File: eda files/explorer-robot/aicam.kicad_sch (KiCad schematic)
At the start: 7 parts, among them J8 AI CAM, U9 TPS22917DBV

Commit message: Add expansion connector sheet and hierarchical wiring
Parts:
- J8: value AI CAM -> AI.CAM
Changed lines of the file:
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@@
 			)
 		)
-		(property "Value" "AI CAM"
+		(property "Value" "AI.CAM"
 			(at 187.96 96.5199 0)
 			(show_name no)

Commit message: ``` Move AI camera branch to 3.3 V rail
The Grove Vision AI V2 module used here requires a 3.3 V input,
so powering it from the switched 5 V branch would over-voltage it.
Point U9 VIN at +3.3V; the TPS22917, footprint and control are
unchanged.

Also bump the 5 V inductor to 15 µH/3 A, swap the catch diode,
clean up schematic wiring and add no-connects on unused pins.
Document the decision in ADR-0025 and update ADR-0019, ADR-0021
and CONTEXT.md.
```
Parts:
- added C60: 10u, Capacitor_SMD:C_0805_2012Metric, symbol Device:C
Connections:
- net GND: now also C60.2
- net at C54.2, J8.1 (Pin_1), R20.1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: now also C60.1
- net +5V renamed +3.3V
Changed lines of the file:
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@@
+	)
+	(junction
+		(at 177.8 91.44)
+		(diameter 0)
+		(color 0 0 0 0)
 	)
 	(junction
@@
 	(wire
 		(pts
+			(xy 177.8 90.17) (xy 177.8 91.44)
+		)
+		(stroke
+			(width 0)
+			(type default)
+		)
+	)
+	(wire
+		(pts
 			(xy 123.19 91.44) (xy 135.89 91.44)
 		)
@@
 	(wire
 		(pts
+			(xy 177.8 80.01) (xy 177.8 82.55)
+		)
+		(stroke
+			(width 0)
+			(type default)
+		)
+	)
+	(wire
+		(pts
+			(xy 177.8 91.44) (xy 180.34 91.44)
+		)
+		(stroke
+			(width 0)
+			(type default)
+		)
+	)
+	(wire
+		(pts
 			(xy 167.64 96.52) (xy 167.64 101.6)
 		)
@@
 	(wire
 		(pts
-			(xy 170.18 91.44) (xy 180.34 91.44)
+			(xy 170.18 91.44) (xy 177.8 91.44)
 		)
 		(stroke
@@
 	)
 	(symbol
+		(lib_id "Device:C")
+		(at 177.8 86.36 180)
+		(unit 1)
+		(body_style 1)
+		(exclude_from_sim no)
+		(in_bom yes)
+		(on_board yes)
+		(in_pos_files yes)
+		(dnp no)
+		(property "Reference" "C60"
+			(at 184.912 87.376 0)
+			(show_name no)
+			(do_not_autoplace no)
+			(effects
+				(font
+					(size 1.27 1.27)
+				)
+				(justify left)
+			)
+		)
+		(property "Value" "10u"
+			(at 184.912 84.836 0)
+			(show_name no)
+			(do_not_autoplace no)
+			(effects
+				(font
+					(size 1.27 1.27)
+				)
+				(justify left)
+			)
+		)
+		(property "Footprint" "Capacitor_SMD:C_0805_2012Metric"
+			(at 176.8348 82.55 0)
+			(hide yes)
+			(show_name no)
+			(do_not_autoplace no)
+			(effects
+				(font
+					(size 1.27 1.27)
+				)
+			)
+		)
+		(property "Datasheet" ""
+			(at 177.8 86.36 0)
+			(hide yes)
+			(show_name no)
+			(do_not_autoplace no)
+			(effects
+				(font
+					(size 1.27 1.27)
+				)
+			)
+		)
+		(property "Description" "Unpolarized capacitor"
+			(at 177.8 86.36 0)
+			(hide yes)
+			(show_name no)
+			(do_not_autoplace no)
+			(effects
+				(font
+					(size 1.27 1.27)
+				)
+			)
+		)
+		(property "JLCPCB_URL" "https://jlcpcb.com/partdetail/16532-CL21A106KAYNNNE/C15850"
+			(at 177.8 86.36 0)
+			(hide yes)
+			(show_name no)
+			(do_not_autoplace no)
+			(effects
+				(font
+					(size 1.27 1.27)
+				)
+			)
+		)
+		(property "LCSC" "C15850"
+			(at 177.8 86.36 0)
+			(hide yes)
+			(show_name no)
+			(do_not_autoplace no)
+			(effects
+				(font
+					(size 1.27 1.27)
+				)
+			)
+		)
+		(property "MFR" "Samsung Electro-Mechanics"
+			(at 177.8 86.36 0)
+			(hide yes)
+			(show_name no)
+			(do_not_autoplace no)
+			(effects
+				(font
+					(size 1.27 1.27)
+				)
+			)
+		)
+		(property "MPN" "CL21A106KAYNNNE"
+			(at 177.8 86.36 0)
+			(hide yes)
+			(show_name no)
+			(do_not_autoplace no)
+			(effects
+				(font
+					(size 1.27 1.27)
+				)
+			)
+		)
+		(pin "2"
+		)
+		(pin "1"
+		)
+		(instances
+			(project "explorer-robot"
+				(path "/57778957-dc0c-4e39-b470-8f64ada5e845/e28148a8-209c-4954-97f4-1069761fd156"
+					(reference "C60")
+					(unit 1)
+				)
+			)
+		)
+	)
+	(symbol
+		(lib_id "power:GND")
+		(at 177.8 80.01 180)
+		(unit 1)
+		(body_style 1)
+		(exclude_from_sim no)
+		(in_bom yes)
+		(on_board yes)
+		(in_pos_files yes)
+		(dnp no)
+		(fields_autoplaced yes)
+		(property "Reference" "#PWR094"
+			(at 177.8 73.66 0)
+			(hide yes)
+			(show_name no)
+			(do_not_autoplace no)
+			(effects
+				(font
+					(size 1.27 1.27)
+				)
+			)
+		)
+		(property "Value" "GND"
+			(at 177.8 74.93 0)
+			(show_name no)
+			(do_not_autoplace no)
+			(effects
+				(font
+					(size 1.27 1.27)
+				)
+			)
+		)
+		(property "Footprint" ""
+			(at 177.8 80.01 0)
+			(hide yes)
+			(show_name no)
+			(do_not_autoplace no)
+			(effects
+				(font
+					(size 1.27 1.27)
+				)
+			)
+		)
+		(property "Datasheet" ""
+			(at 177.8 80.01 0)
+			(hide yes)
+			(show_name no)
+			(do_not_autoplace no)
+			(effects
+				(font
+					(size 1.27 1.27)
+				)
+			)
+		)
+		(property "Description" "Power symbol creates a global label with name \"GND\" , ground"
+			(at 177.8 80.01 0)
+			(hide yes)
+			(show_name no)
+			(do_not_autoplace no)
+			(effects
+				(font
+					(size 1.27 1.27)
+				)
+			)
+		)
+		(pin "1"
+		)
+		(instances
+			(project "explorer-robot"
+				(path "/57778957-dc0c-4e39-b470-8f64ada5e845/e28148a8-209c-4954-97f4-1069761fd156"
+					(reference "#PWR094")
+					(unit 1)
+				)
+			)
+		)
+	)
+	(symbol
 		(lib_id "Device:R")
 		(at 160.02 91.44 270)
@@
 	)
 	(symbol
-		(lib_id "power:+5V")
+		(lib_id "power:+3.3V")
 		(at 124.46 86.36 90)
 		(unit 1)
@@
 		(in_pos_files yes)
 		(dnp no)
-		(fields_autoplaced yes)
 		(property "Reference" "#PWR078"
 			(at 128.27 86.36 0)
@@
 			)
 		)
-		(property "Value" "+5V"
-			(at 119.38 86.36 0)
+		(property "Value" "+3.3V"
+			(at 117.602 86.614 90)
 			(show_name no)
 			(do_not_autoplace no)
@@
 			)
 		)
-		(property "Description" "Power symbol creates a global label with name \"+5V\""
+		(property "Description" "Power symbol creates a global label with name \"+3.3V\""
 			(at 124.46 86.36 0)
 			(hide yes)

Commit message: Update AI camera branch to 5V and document schematic
- ADR-0027 supersedes ADR-0025: AI camera input is 5V, not 3.3V
- Move U9 VIN and C55 back to +5V in aicam.kicad_sch
- Update CONTEXT.md branch descriptions and ADR cross-references
- Record ICM-20948 placement status and corrected battery divider ratio
- Adjust battery_charge_read for 33k/10k divider (0.2326 ratio)
- Enable sheet component classes; refresh netlist and PCB footprints
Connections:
- net +3.3V renamed +5V
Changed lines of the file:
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@@
+	)
+	(symbol
+		(lib_id "power:+5V")
+		(at 124.46 86.36 90)
+		(unit 1)
+		(body_style 1)
+		(exclude_from_sim no)
+		(in_bom yes)
+		(on_board yes)
+		(in_pos_files yes)
+		(dnp no)
+		(fields_autoplaced yes)
+		(property "Reference" "#PWR078"
+			(at 128.27 86.36 0)
+			(hide yes)
+			(show_name no)
+			(do_not_autoplace no)
+			(effects
+				(font
+					(size 1.27 1.27)
+				)
+			)
+		)
+		(property "Value" "+5V"
+			(at 120.65 86.3599 90)
+			(show_name no)
+			(do_not_autoplace no)
+			(effects
+				(font
+					(size 1.27 1.27)
+				)
+				(justify left)
+			)
+		)
+		(property "Footprint" ""
+			(at 124.46 86.36 0)
+			(hide yes)
+			(show_name no)
+			(do_not_autoplace no)
+			(effects
+				(font
+					(size 1.27 1.27)
+				)
+			)
+		)
+		(property "Datasheet" ""
+			(at 124.46 86.36 0)
+			(hide yes)
+			(show_name no)
+			(do_not_autoplace no)
+			(effects
+				(font
+					(size 1.27 1.27)
+				)
+			)
+		)
+		(property "Description" "Power symbol creates a global label with name \"+5V\""
+			(at 124.46 86.36 0)
+			(hide yes)
+			(show_name no)
+			(do_not_autoplace no)
+			(effects
+				(font
+					(size 1.27 1.27)
+				)
+			)
+		)
+		(pin "1"
+		)
+		(instances
+			(project "explorer-robot"
+				(path "/57778957-dc0c-4e39-b470-8f64ada5e845/e28148a8-209c-4954-97f4-1069761fd156"
+					(reference "#PWR078")
+					(unit 1)
+				)
+			)
+		)
 	)
 	(symbol
@@
 					(unit 1)
 				)
-			)
-		)
-	)
-	(symbol
-		(lib_id "power:+3.3V")
-		(at 124.46 86.36 90)
-		(unit 1)
-		(body_style 1)
-		(exclude_from_sim no)
-		(in_bom yes)
-		(on_board yes)
-		(in_pos_files yes)
-		(dnp no)
-		(property "Reference" "#PWR078"
-			(at 128.27 86.36 0)
-			(hide yes)
-			(show_name no)
-			(do_not_autoplace no)
-			(effects
-				(font
-					(size 1.27 1.27)
-				)
-			)
-		)
-		(property "Value" "+3.3V"
-			(at 117.602 86.614 90)
-			(show_name no)
-			(do_not_autoplace no)
-			(effects
-				(font
-					(size 1.27 1.27)
-				)
-			)
-		)
-		(property "Footprint" ""
-			(at 124.46 86.36 0)
-			(hide yes)
-			(show_name no)
-			(do_not_autoplace no)
-			(effects
-				(font
-					(size 1.27 1.27)
-				)
-			)
-		)
-		(property "Datasheet" ""
-			(at 124.46 86.36 0)
-			(hide yes)
-			(show_name no)
-			(do_not_autoplace no)
-			(effects
-				(font
-					(size 1.27 1.27)
-				)
-			)
-		)
-		(property "Description" "Power symbol creates a global label with name \"+3.3V\""
-			(at 124.46 86.36 0)
-			(hide yes)
-			(show_name no)
-			(do_not_autoplace no)
-			(effects
-				(font
-					(size 1.27 1.27)
-				)
-			)
-		)
-		(pin "1"
-		)
-		(instances
-			(project "explorer-robot"
-				(path "/57778957-dc0c-4e39-b470-8f64ada5e845/e28148a8-209c-4954-97f4-1069761fd156"
-					(reference "#PWR078")
-					(unit 1)
-				)

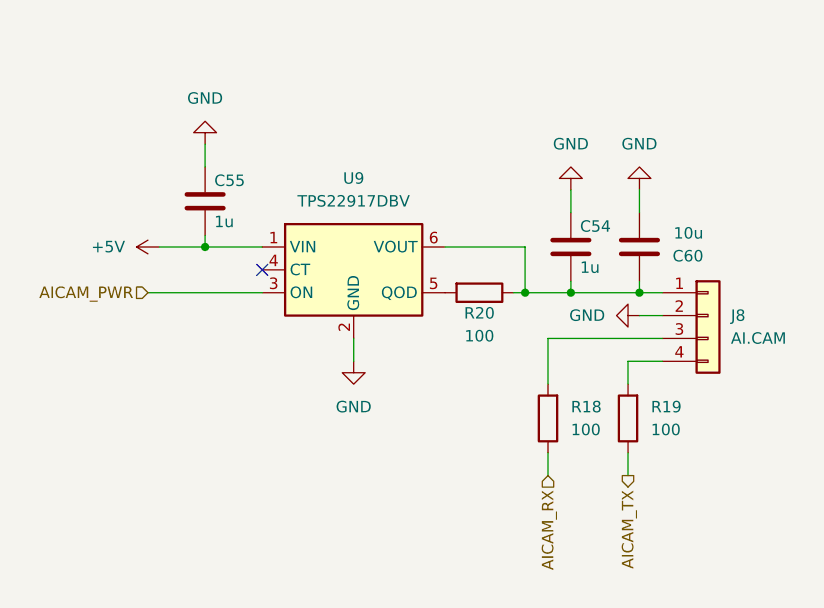
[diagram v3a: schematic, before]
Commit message: Add 1 nF CT capacitors to TPS22917 load switches
Specify C29/C30/C67/C68 on the LiDAR, AI camera, expansion and
panel branches to give a controlled rise and limit inrush. Update
ADRs 0010, 0021, 0024 and 0027 and CONTEXT.md to match, rework the
affected schematics, and swap the inductor footprint to the
EasyEDA SLO0618H part.
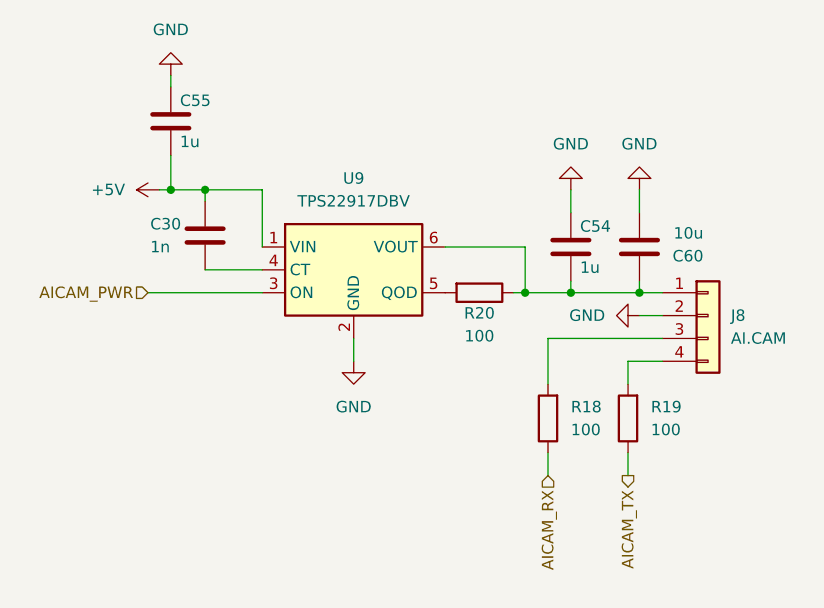
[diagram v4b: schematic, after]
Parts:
- added C30: 1n, Capacitor_SMD:C_0603_1608Metric, symbol Device:C
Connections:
- net +5V: now also C30.2
- net at U9.4 (CT): now also C30.1
- no-connect marks 1 -> 0
